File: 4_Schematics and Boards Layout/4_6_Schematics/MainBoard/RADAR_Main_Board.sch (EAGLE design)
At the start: 791 parts, among them IC1 AT93C46A-10SQ-2.7, J1 142-0731-211, J18 142-0731-211, J19 CJT-T-P-HH-ST-TH1, J20 142-0731-211, J21 CJT-T-P-HH-ST-TH1, J22 142-0731-211, J23 142-0731-211, J24 142-0731-211, J25 142-0731-211, J26 142-0731-211, J27 142-0731-211, J28 142-0731-211, J29 142-0731-211, J30 142-0731-211, J31 142-0731-211, J32 142-0731-211, J33 142-0731-211, J34 142-0731-211, J35 142-0731-211, J36 142-0731-211, J37 142-0731-211, J38 142-0731-211, J39 142-0731-211, J40 142-0731-211, J41 142-0731-211, J42 142-0731-211, J43 142-0731-211, J44 142-0731-211, J45 142-0731-211, J46 142-0731-211, J47 142-0731-211, J48 142-0731-211, J49 142-0731-211, J50 142-0731-211, J51 142-0731-211, J52 142-0731-211, J53 142-0731-211, J54 142-0731-211, J55 142-0731-211, U1 AD9484BCPZ-500, U10 ADS7830IPWR, U11 INA241A4IDGKRDGK0008A-MFG, U13 LTC5552IUDBTRMPBF, U14 SZMMSZ5232BT1G, U15 SZMMSZ5232BT1G, U16 EP4RKU+, U17 SZMMSZ5232BT1G, U2 STM32F746ZGT7, U3 AD9708AR, U37 SZMMSZ5232BT1G, U38 SZMMSZ5232BT1G, U39 SZMMSZ5232BT1G, U4 AD8352ACPZ-R7, U40 SZMMSZ5232BT1G, U41 SZMMSZ5232BT1G, U42 XC7A50T-2FTG256I, U43 SZMMSZ5232BT1G, U44 SZMMSZ5232BT1G, U45 SZMMSZ5232BT1G, U46 SZMMSZ5232BT1G, U47 SZMMSZ5232BT1G, U48 SZMMSZ5232BT1G, U49 SZMMSZ5232BT1G, U5 LTC5552IUDBTRMPBF, U50 SZMMSZ5232BT1G, U51 SZMMSZ5232BT1G, U52 SZMMSZ5232BT1G, U53 SZMMSZ5232BT1G, U54 SZMMSZ5232BT1G, U55 SZMMSZ5232BT1G, U56 SZMMSZ5232BT1G, U57 SZMMSZ5232BT1G, U58 SZMMSZ5232BT1G, U59 SZMMSZ5232BT1G, U6 FT2232HQ, U60 SZMMSZ5232BT1G, U61 SZMMSZ5232BT1G, U62 SZMMSZ5232BT1G, U63 SZMMSZ5232BT1G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

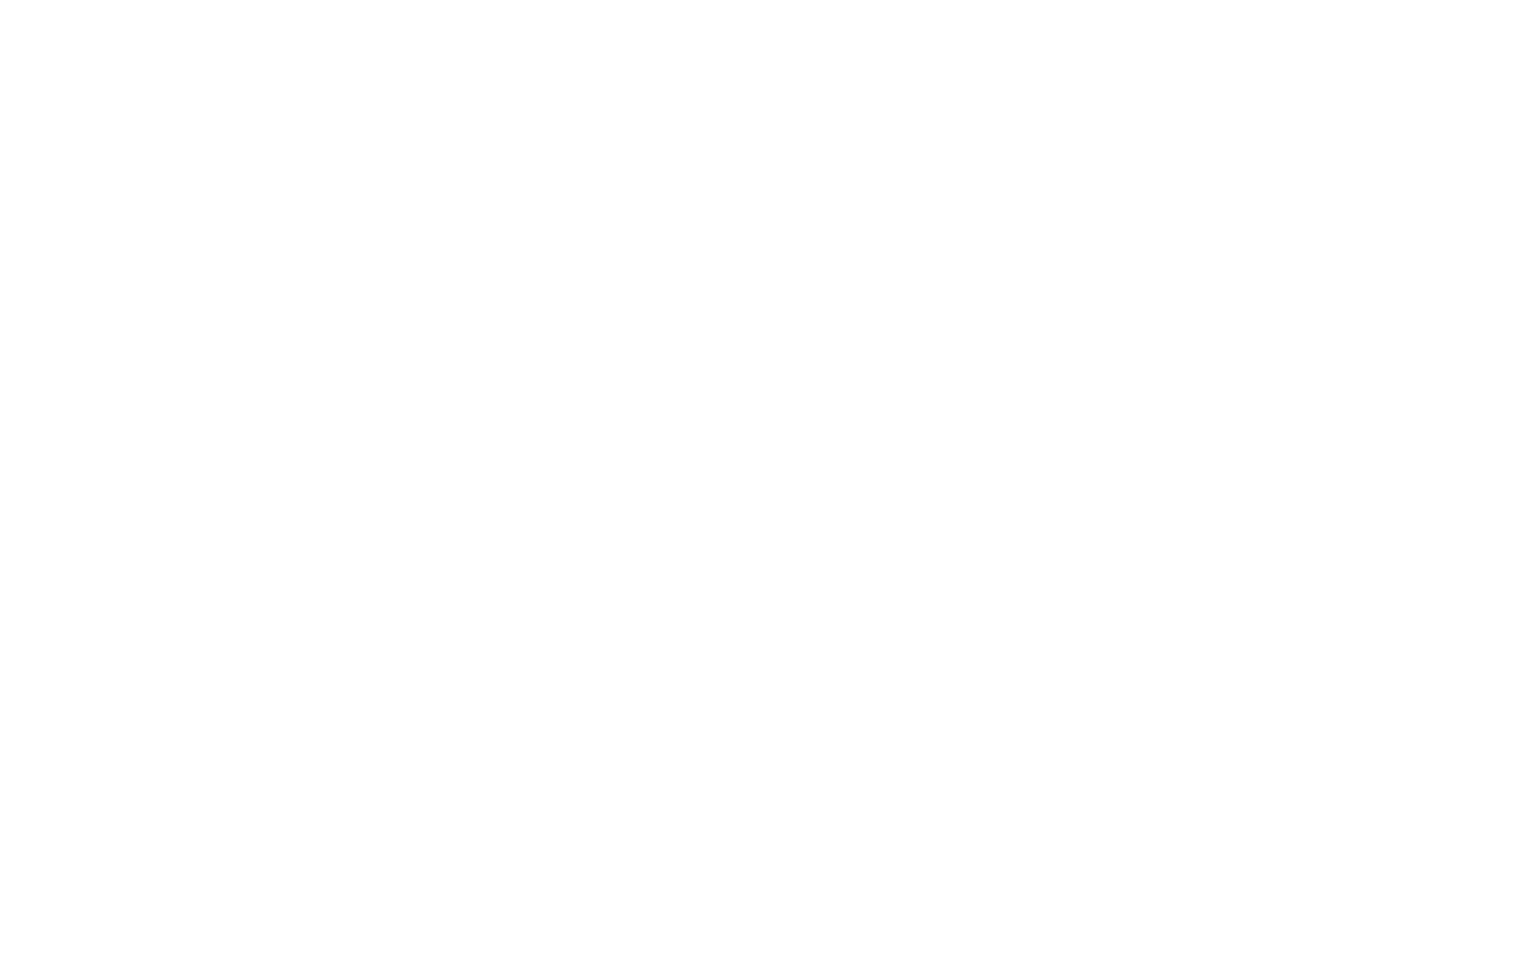
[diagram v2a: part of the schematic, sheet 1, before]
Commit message: feat(hw): cavity-filter interface on the main board (Lane B B1.3)
Decision (owner): cavity filters rather than microstrip, because >= 40 dB of image
rejection 240 MHz from a 10.5 GHz passband is not a microstrip-with-tuning job.
The filter is therefore off-board, which means the board needs launches and the
two 2-pin `BPF2` placeholders (`U$2`, `U$3`) no longer represent anything.

Added, using only devices that already exist in the repo's libraries:

    4 x SMA jack `142-0731-211`   (J56-J59)  -- the deviceset, symbol and
                                              package were already present
    2 x 0R bridge                 (R174, R175) -- R-EU_ R0201, MPN copied from
                                              the existing 0R parts (R18/R19/
                                              R34/R35 -> RCA02010000ZSEDSR)

Topology: one launch at each end of each off-board filter -- J56 on RF_TX_FIL,
J57 on RF_TX, J58 on RF_RX, J59 on RF_RX_FIL -- with the SMA legs (pads 2-5) on
GND, and a 0R across each pair as the bench bypass so the chain can be brought up
without the filters.  The placeholders are removed rather than left in the signal
path, together with their board contactrefs.

Placement was searched, not guessed: for each new part the closest free position
to its anchor that keeps clearance from every existing element (6.5 mm for the
SMA jacks, 2.2 mm for the resistors) -- achieved 6.6-14.2 mm and 2.7-5.6 mm, and
the pairs stay 13-21 mm apart so a bolt-on cavity can reach both ports.

Verified: both CAD files parse with the expected structure (1982 parts / 795
elements, i.e. -2 placeholders +6 parts), no `U$2`/`U$3` reference survives on
this board, each RF net carries its original part plus the launch centre pin and
one bridge pin, the RF sheet's GND gains the 16 SMA leg pins, and all three
artifact gates are green -- the board/BOM gate is what proves the three files
agree.  DNP_list.csv regenerated: the two placeholders give way to the two
bench-bypass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
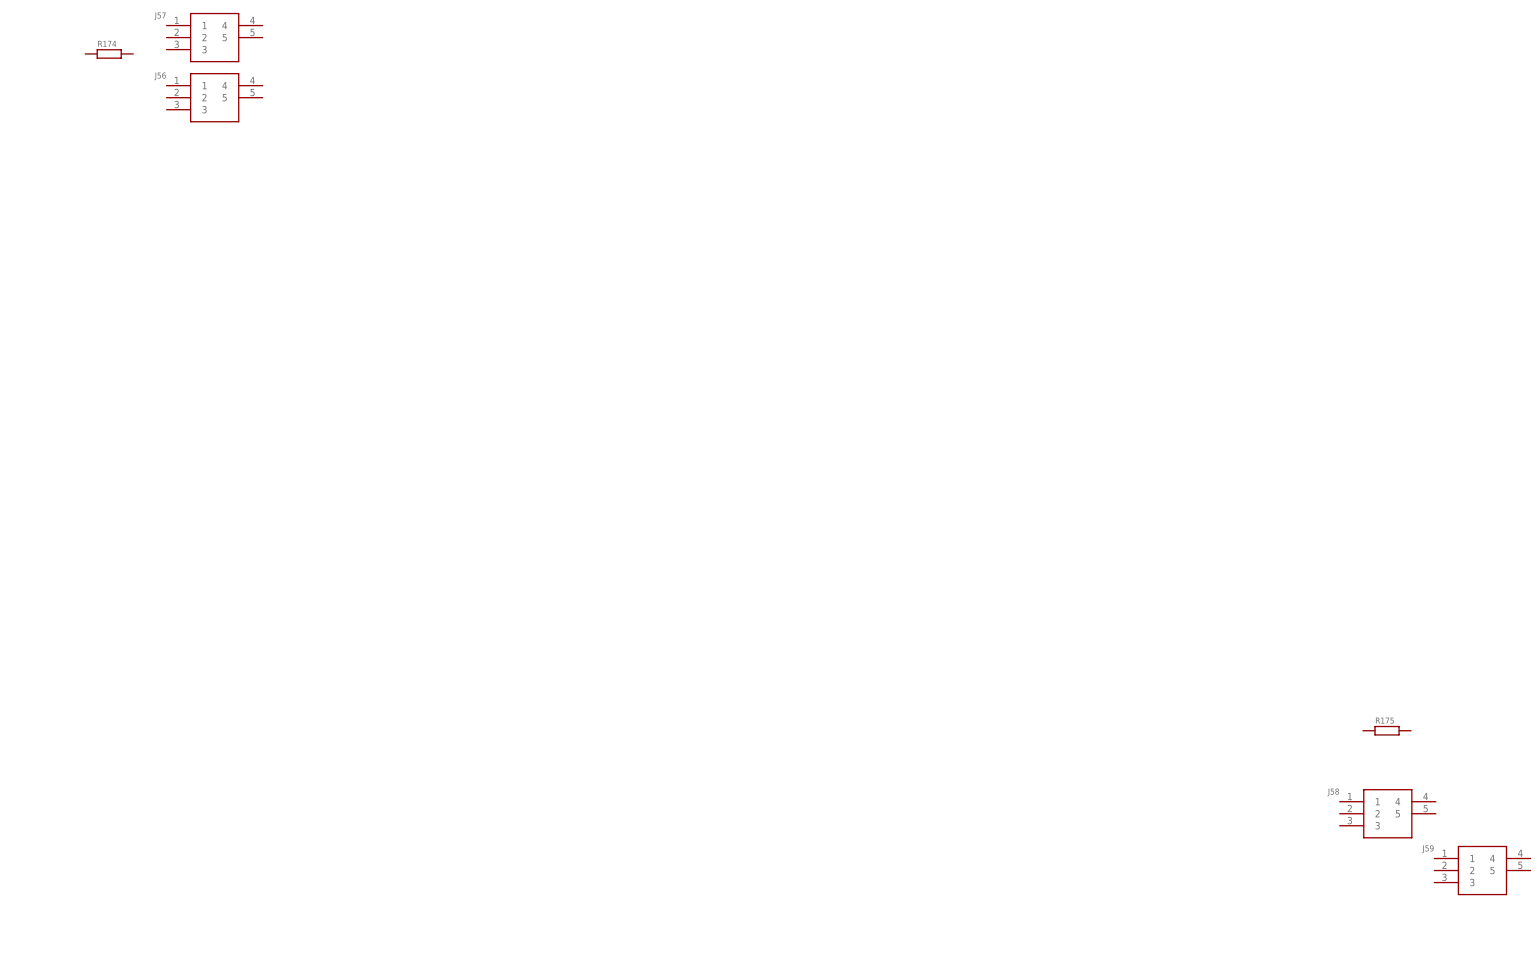
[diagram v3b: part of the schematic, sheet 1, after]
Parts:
- removed U$2, U$3: BPF2, My_Library_RADAR:BPF2
- added J56, J57, J58, J59: 142-0731-211, 142-0731-211:142-0731-211
- added R174, R175: 0R, rcl:R-EU_R0201
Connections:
- net GND: now also J56.2, J56.3, J56.4, J56.5, J57.2, J57.3, J57.4, J57.5, J58.2, J58.3, J58.4, J58.5, J59.2, J59.3, J59.4, J59.5
- net RF_RX: now also J58.1, R175.1; no longer U$3.IN
- net RF_RX_FIL: now also J59.1, R175.2; no longer U$3.OUT
- net RF_TX: now also J57.1, R174.2; no longer U$2.OUT
- net RF_TX_FIL: now also J56.1, R174.1; no longer U$2.IN
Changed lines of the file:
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@@
 <part name="R146" library="eagle-ltspice" deviceset="R" device="R0201" value="2.2k"/>
 <part name="GND754" library="supply1" deviceset="GND" device=""/>
-<part name="C159" library="eagle-ltspice" deviceset="C" device="C0201" value="0.1uF"/>
-<part name="U$2" library="My_Library_RADAR" deviceset="BPF2" device=""/>
-<part name="U$3" library="My_Library_RADAR" deviceset="BPF2" device=""/>
+<part name="C159" library="eagle-ltspice" deviceset="C" device="C0201" value="0.1uF"/><part name="J56" library="142-0731-211" deviceset="142-0731-211" device=""/><part name="J57" library="142-0731-211" deviceset="142-0731-211" device=""/><part name="J58" library="142-0731-211" deviceset="142-0731-211" device=""/><part name="J59" library="142-0731-211" deviceset="142-0731-211" device=""/><part name="R174" library="rcl" deviceset="R-EU_" device="R0201" value="0R"/><part name="R175" library="rcl" deviceset="R-EU_" device="R0201" value="0R"/>
 <part name="L22" library="eagle-ltspice" deviceset="L" device="L0201" value="107.3nH"/>
 <part name="C127" library="eagle-ltspice" deviceset="C" device="C0201" value="32.8pF"/>
@@
 </plain>
 <instances>
-<instance part="X4" gate="-1" x="83.82" y="210.82" smashed="yes">
+<instance part="J56" gate="G$1" x="452.12" y="241.3" smashed="yes"><attribute name="NAME" x="449.62" y="242.8" size="1.27" layer="95"/></instance><instance part="J57" gate="G$1" x="452.12" y="254.0" smashed="yes"><attribute name="NAME" x="449.62" y="255.5" size="1.27" layer="95"/></instance><instance part="J58" gate="G$1" x="700.0" y="90.0" smashed="yes"><attribute name="NAME" x="697.5" y="91.5" size="1.27" layer="95"/></instance><instance part="J59" gate="G$1" x="720.0" y="78.0" smashed="yes"><attribute name="NAME" x="717.5" y="79.5" size="1.27" layer="95"/></instance><instance part="R174" gate="G$1" x="440.0" y="248.0" smashed="yes"><attribute name="NAME" x="437.5" y="249.5" size="1.27" layer="95"/></instance><instance part="R175" gate="G$1" x="710.0" y="105.0" smashed="yes"><attribute name="NAME" x="707.5" y="106.5" size="1.27" layer="95"/></instance><instance part="X4" gate="-1" x="83.82" y="210.82" smashed="yes">
 <attribute name="NAME" x="86.36" y="210.058" size="1.524" layer="95"/>
 <attribute name="VALUE" x="83.058" y="212.217" size="1.778" layer="96"/>
@@
 <attribute name="VALUE" x="556.26" y="429.26" size="1.778" layer="96" rot="R90"/>
 </instance>
-<instance part="U$2" gate="G$1" x="452.12" y="241.3" smashed="yes">
-<attribute name="NAME" x="449.58" y="254" size="1.27" layer="95"/>
-<attribute name="VALUE" x="449.58" y="231.14" size="1.27" layer="96"/>
-</instance>
-<instance part="U$3" gate="G$1" x="728.98" y="101.6" smashed="yes">
-<attribute name="NAME" x="726.44" y="114.3" size="1.27" layer="95"/>
-<attribute name="VALUE" x="726.44" y="91.44" size="1.27" layer="96"/>
-</instance>
 <instance part="L22" gate="G$1" x="269.24" y="251.46" smashed="yes" rot="R90">
 <attribute name="NAME" x="273.05" y="249.9614" size="1.778" layer="95" rot="R180"/>
@@
 <pinref part="C353" gate="G$1" pin="2"/>
 <pinref part="GND1099" gate="1" pin="GND"/>
-</segment>
+<segment><pinref part="J56" gate="G$1" pin="2"/><pinref part="J56" gate="G$1" pin="3"/><pinref part="J56" gate="G$1" pin="4"/><pinref part="J56" gate="G$1" pin="5"/><pinref part="J57" gate="G$1" pin="2"/><pinref part="J57" gate="G$1" pin="3"/><pinref part="J57" gate="G$1" pin="4"/><pinref part="J57" gate="G$1" pin="5"/><pinref part="J58" gate="G$1" pin="2"/><pinref part="J58" gate="G$1" pin="3"/><pinref part="J58" gate="G$1" pin="4"/><pinref part="J58" gate="G$1" pin="5"/><pinref part="J59" gate="G$1" pin="2"/><pinref part="J59" gate="G$1" pin="3"/><pinref part="J59" gate="G$1" pin="4"/><pinref part="J59" gate="G$1" pin="5"/></segment></segment>
 </net>
 <net name="+5V0_PA_1" class="0">
@@
 <segment>
 <label x="698.5" y="104.14" size="1.778" layer="95"/>
-<pinref part="U$3" gate="G$1" pin="IN"/>
+<pinref part="J58" gate="G$1" pin="1"/>
 <wire x1="713.74" y1="104.14" x2="706.12" y2="104.14" width="0.1524" layer="91"/>
-</segment>
+<pinref part="R175" gate="G$1" pin="1"/></segment>
 </net>
 <net name="MIX_RX_EN" class="0">
@@
 <segment>
 <label x="472.44" y="243.84" size="1.778" layer="95"/>
-<pinref part="U$2" gate="G$1" pin="OUT"/>
+<pinref part="J57" gate="G$1" pin="1"/>
 <wire x1="472.44" y1="243.84" x2="467.36" y2="243.84" width="0.1524" layer="91"/>
-</segment>
+<pinref part="R174" gate="G$1" pin="2"/></segment>
 </net>
 <net name="MIX_TX_EN" class="0">
@@
 <segment>
 <label x="421.64" y="243.84" size="1.778" layer="95"/>
-<pinref part="U$2" gate="G$1" pin="IN"/>
+<pinref part="J56" gate="G$1" pin="1"/>
 <wire x1="429.26" y1="243.84" x2="436.88" y2="243.84" width="0.1524" layer="91"/>
-</segment>
+<pinref part="R174" gate="G$1" pin="1"/></segment>
 </net>
 <net name="RF_IO" class="2">
@@
 <segment>
 <label x="749.3" y="104.14" size="1.778" layer="95"/>
-<pinref part="U$3" gate="G$1" pin="OUT"/>
+<pinref part="J59" gate="G$1" pin="1"/>
 <wire x1="749.3" y1="104.14" x2="744.22" y2="104.14" width="0.1524" layer="91"/>
-</segment>
+<pinref part="R175" gate="G$1" pin="2"/></segment>
 </net>
 <net name="RF_IO_2" class="2">
